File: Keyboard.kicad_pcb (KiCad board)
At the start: 2 copper layers, 404 x 118.3 mm, 226 parts, among them SW2 RotaryEncoder_Switch_MP, U1 MCP23017_SO, U2 MCP23017_SO, U3 Seeeduino Xiao nRF52840

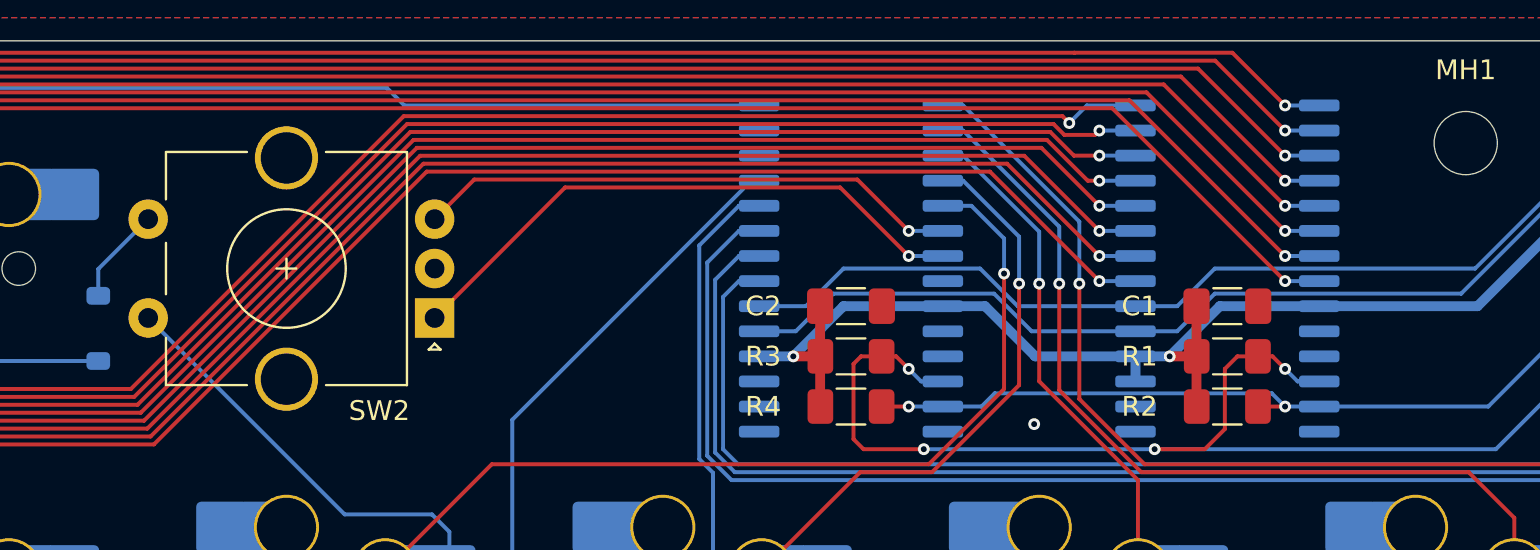
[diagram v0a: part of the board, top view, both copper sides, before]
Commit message: Replaced Rotary Encoder.
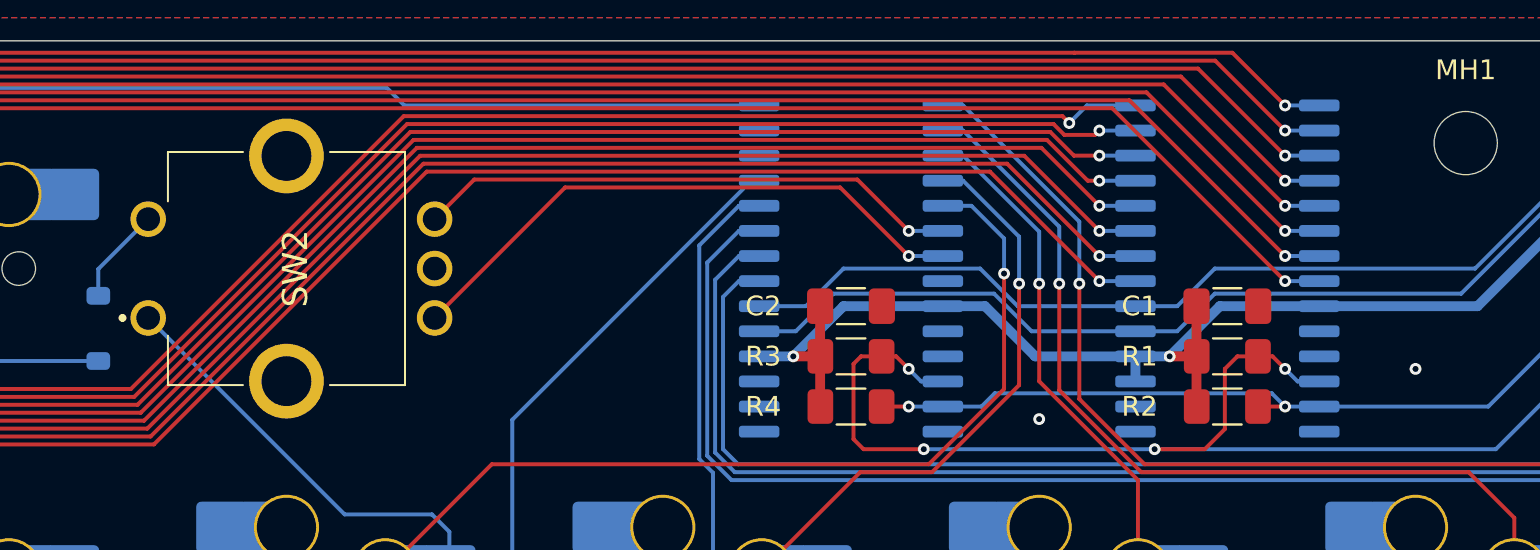
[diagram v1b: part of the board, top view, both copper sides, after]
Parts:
- SW2: footprint Rotary_Encoder:RotaryEncoder_Alps_EC11E-Switch_Vertical_H20mm_CircularMountingHoles -> SamacSys_Parts:PEC11L4115FS0020
- moved SW2 14.5 mm to (335.9, 40.6), turned to 90 degrees
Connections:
- U3 pad 12: MISO -> unconnected-(U3-P1.14-Pad12)_1
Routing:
- net GND: vias 1 -> 2

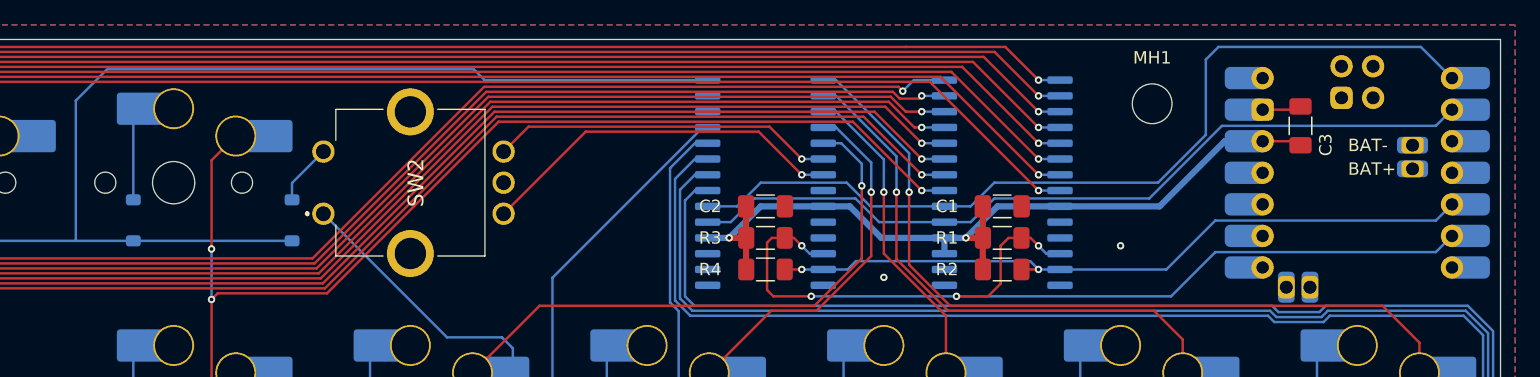
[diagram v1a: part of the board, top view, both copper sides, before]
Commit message: Changed routing.
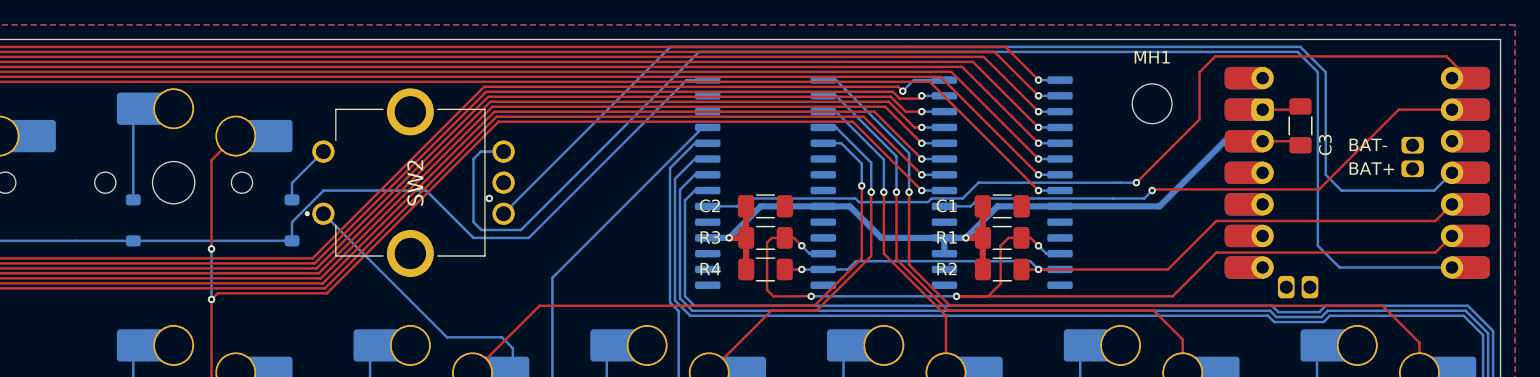
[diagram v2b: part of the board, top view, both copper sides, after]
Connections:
- U1 pad 19: Net-(U1-INTB) -> unconnected-(U1-INTB-Pad19)
- U2 pad 19: Net-(U1-INTB) -> unconnected-(U2-INTB-Pad19)
- U2 pad 20: Net-(U1-INTA) -> Net-(U2-INTA)
- U2 pad 6: ROT_B -> unconnected-(U2-GPB5-Pad6)
- U2 pad 7: ROT_A -> unconnected-(U2-GPB6-Pad7)
- U3 pad 1: Net-(U1-INTA) -> Net-(U2-INTA)
- U3 pad 2: Net-(U1-INTB) -> Net-(U1-INTA)
- U3 pad 4: unconnected-(U3-P0.29-Pad4)_1 -> ROT_A
- U3 pad 7: unconnected-(U3-P1.11-Pad7) -> ROT_B
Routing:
- net ROT_B: track 27.6 -> 109.4 mm, vias 1 -> 0
- net Net-(U2-INTA): track 0.00 -> 69.4 mm, vias 0 -> 1
- net Net-(U1-INTB): track 65.2 -> 0.00 mm
- net ROT_A: track 29.9 -> 92.1 mm, vias 1 -> 0
- net Net-(U1-INTA): track 71.4 -> 44.1 mm, vias 0 -> 1
- net Row 0: track 362.1 -> 341.4 mm
- net SDA: track 57.8 -> 59.5 mm
- net GND: vias 2 -> 1
